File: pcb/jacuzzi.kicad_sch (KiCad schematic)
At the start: 56 parts, among them J1 Conn_01x02, J2 Conn_01x04, J3 Conn_01x03, J4 Conn_01x04, J5 Conn_01x03, J6 Conn_01x03, J7 Conn_01x02, J8 Conn_01x08, K1 G5LE-1, Q1 IRF4905, Q2 BC547, Q3 BC547, Q4 IRF4905, Q5 BC547, Q6 BC547

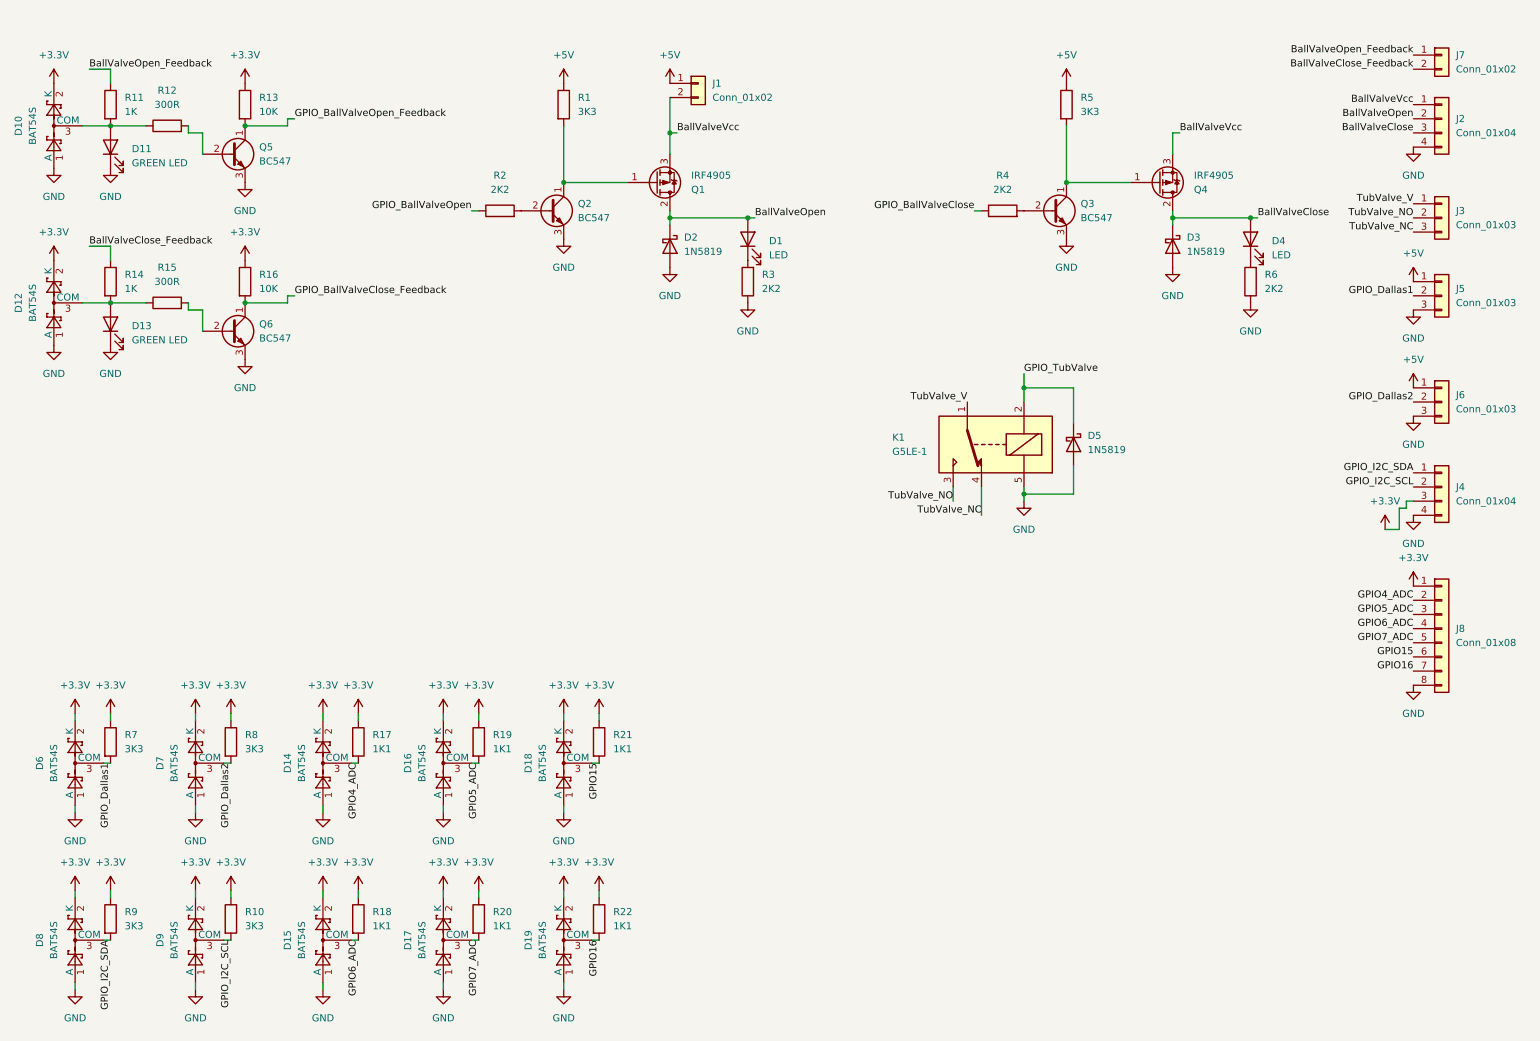
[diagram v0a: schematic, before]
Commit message: now using l293dd
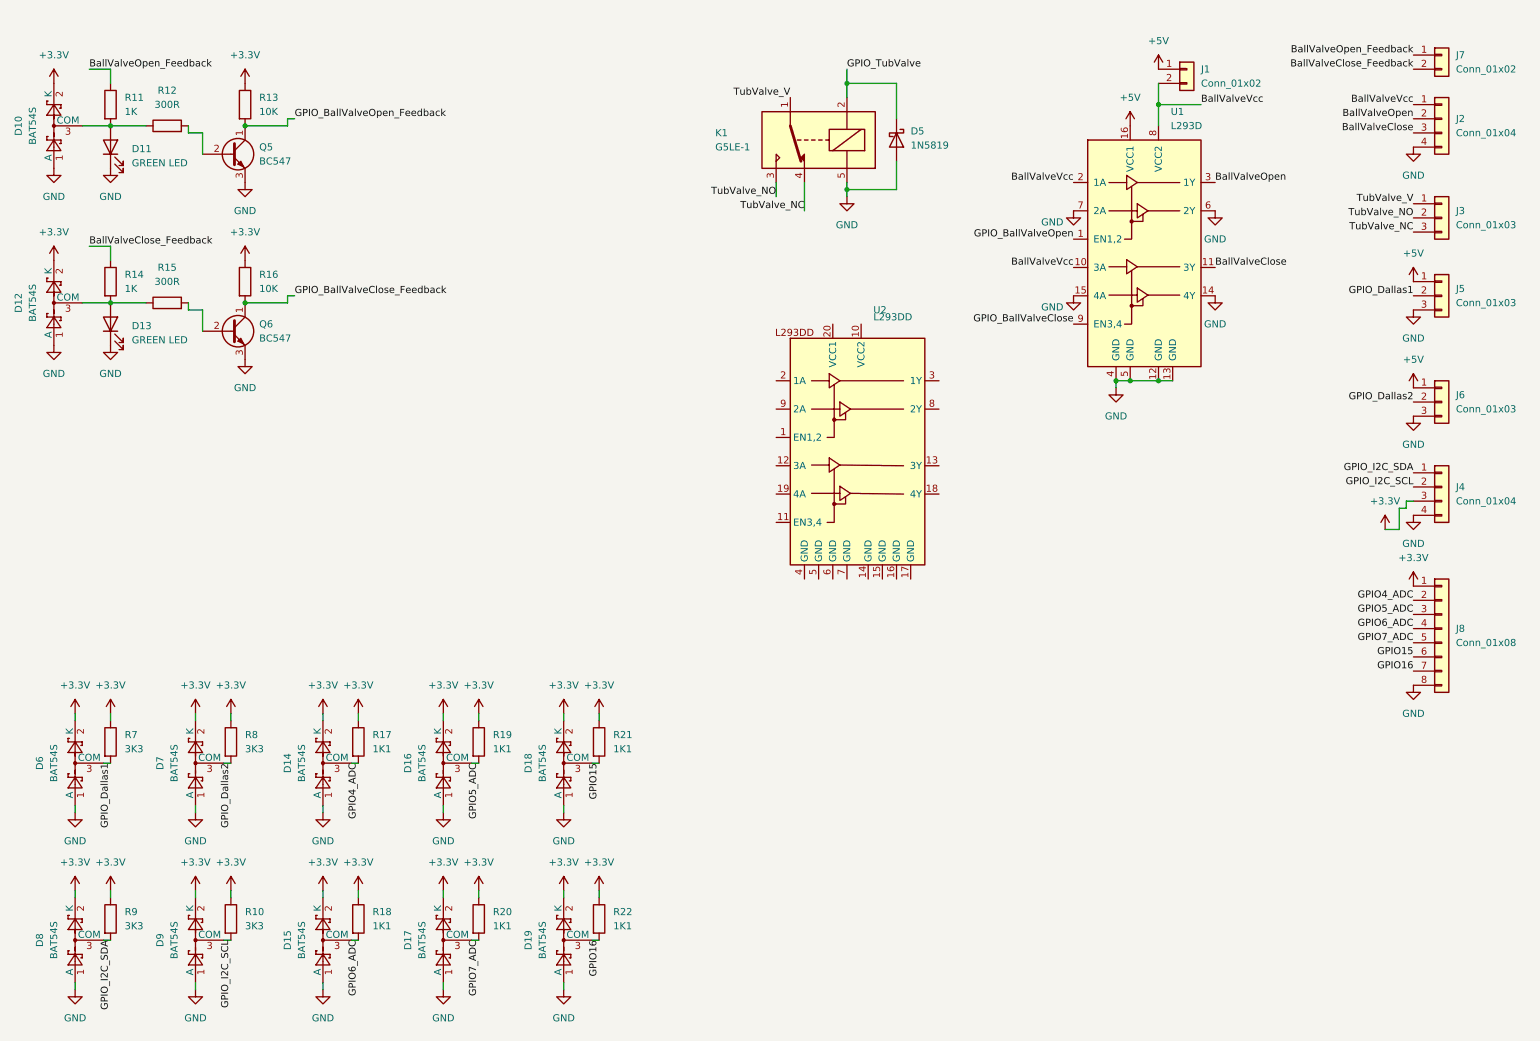
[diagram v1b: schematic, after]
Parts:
- removed D1, D4: LED, symbol Device:LED
- removed D2, D3: 1N5819, Diode_SMD:D_SOD-323, symbol Device:D_Schottky
- removed Q1, Q4: IRF4905, Package_TO_SOT_THT:TO-220-3_Vertical, symbol Transistor_FET:IRF4905
- removed Q2, Q3: BC547, Package_TO_SOT_THT:TO-92_Inline, symbol Transistor_BJT:BC547
- removed R1, R5: 3K3, Resistor_SMD:R_0805_2012Metric, symbol Device:R
- removed R2, R3, R4, R6: 2K2, Resistor_SMD:R_0805_2012Metric, symbol Device:R
- added U1: L293D, Package_SO:SOIC-20W_7.5x12.8mm_P1.27mm, symbol Driver_Motor:L293D
- added U2: L293DD, Package_SO:SOIC-20W_7.5x12.8mm_P1.27mm, symbol my_custom_library:L293DD
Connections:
- net +5V: now also U1.16 (VCC1)
- net BallValveClose: now also U1.11 (3Y)
- net BallValveOpen: now also U1.3 (1Y)
- net BallValveVcc: now also U1.10 (3A), U1.2 (1A), U1.8 (VCC2)
- net GND: now also U1.12 (GND), U1.13 (GND), U1.14 (4Y), U1.15 (4A), U1.4 (GND), U1.5 (GND), U1.6 (2Y), U1.7 (2A)
- net GPIO_BallValveClose: now also U1.9 (EN3,4)
- net GPIO_BallValveOpen: now also U1.1 (EN1,2)
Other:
- moved on the sheet: D5, K1

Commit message: testing if fymbols and foot print work when added to project
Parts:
- added U3: ESP32-DEVKITC-32U, ESP32-DEVKITC-32U:MODULE_ESP32-DEVKITC-32U, symbol ESP32-DEVKITC-32U:ESP32-DEVKITC-32U

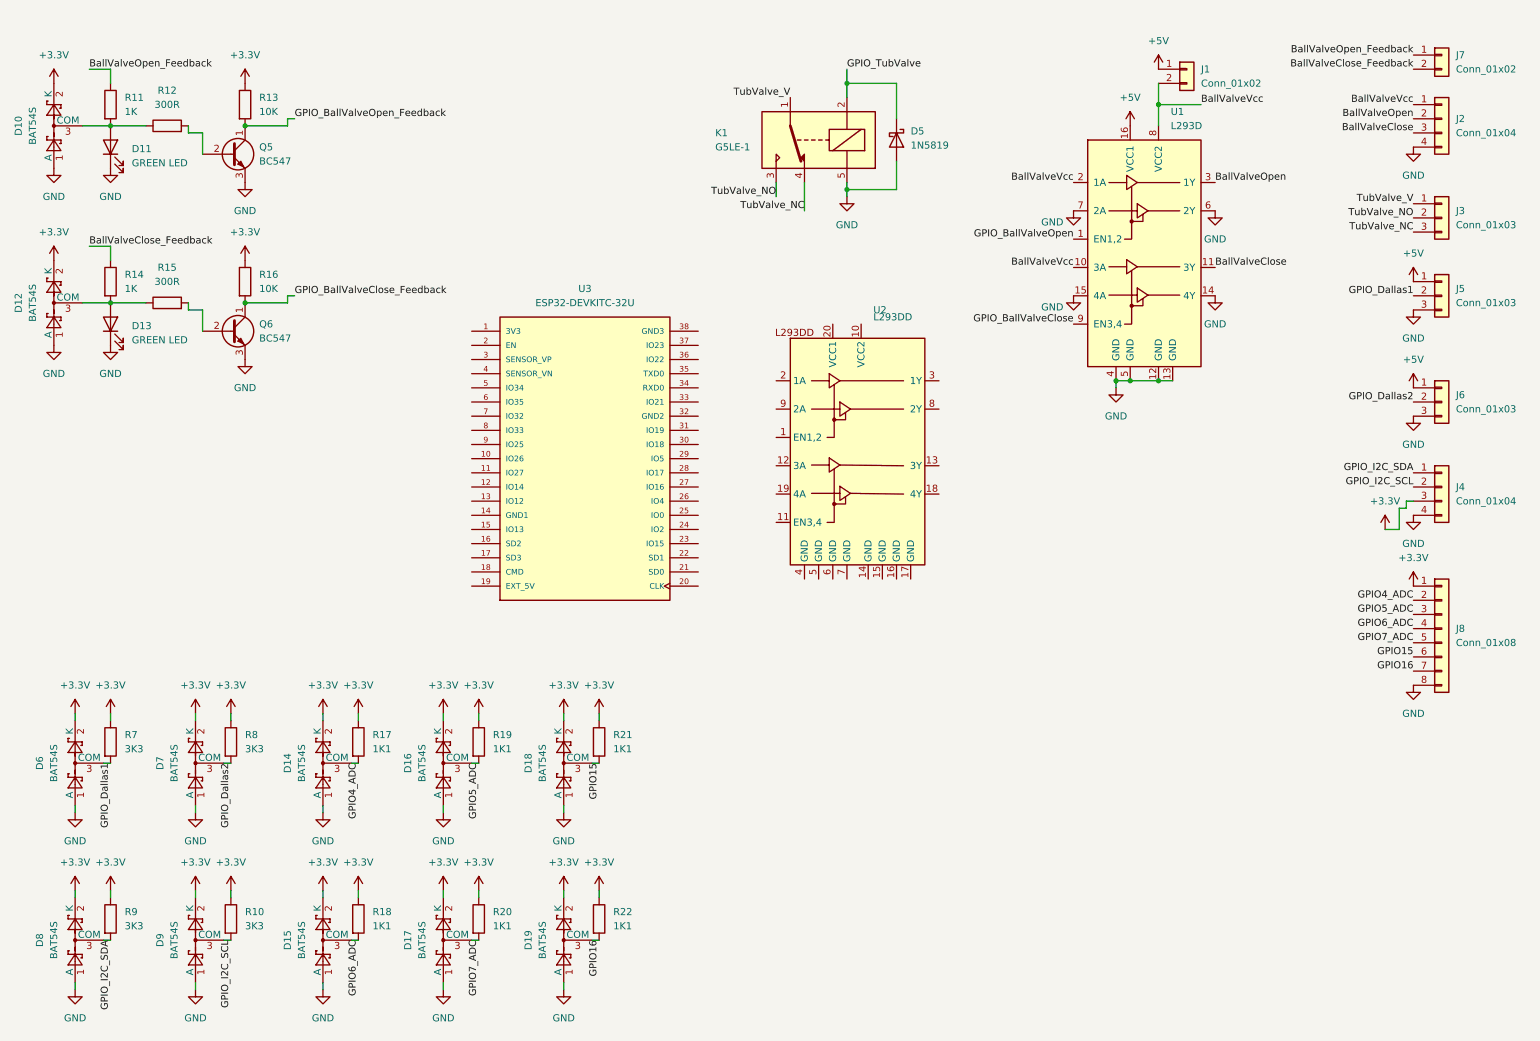
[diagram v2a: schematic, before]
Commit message: use cheap p channels instead of motor circuit, add usb c, add buck converter, switch to smd bjts
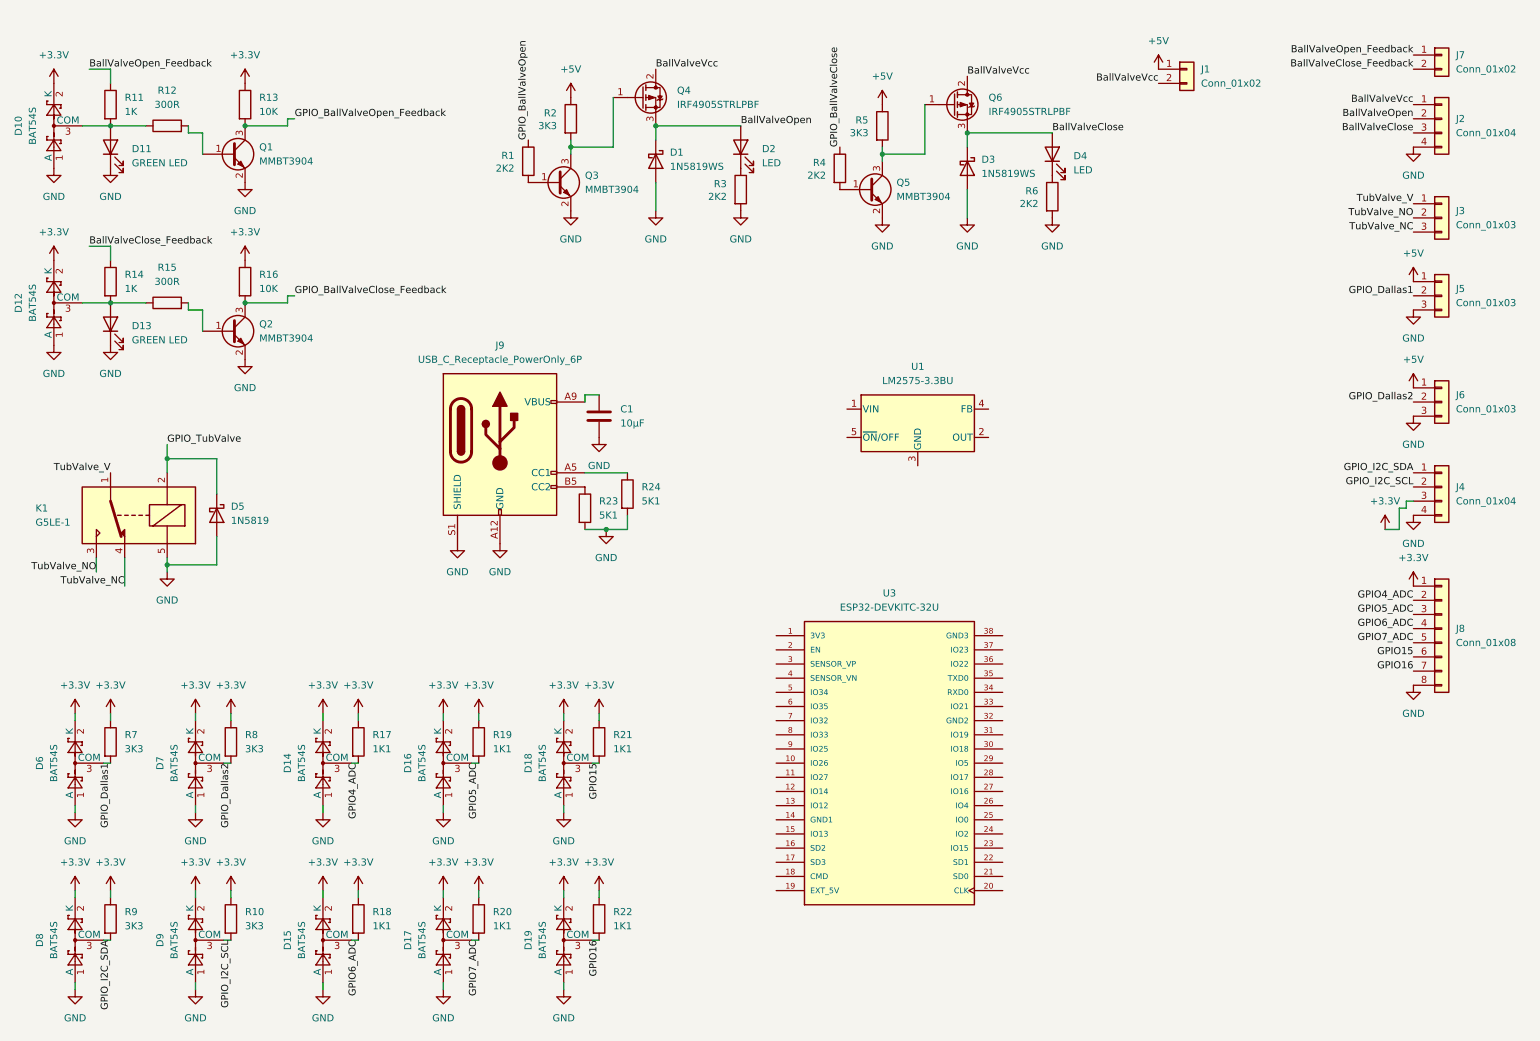
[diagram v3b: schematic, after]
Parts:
- removed Q5, Q6: BC547, Package_TO_SOT_THT:TO-92_Inline, symbol Transistor_BJT:BC547
- removed U1: L293D, Package_SO:SOIC-20W_7.5x12.8mm_P1.27mm, symbol Driver_Motor:L293D
- removed U2: L293DD, Package_SO:SOIC-20W_7.5x12.8mm_P1.27mm, symbol my_custom_library:L293DD
- added C1: 10µF, Capacitor_SMD:C_0805_2012Metric, symbol Device:C
- added D1, D3: 1N5819WS, Diode_SMD:D_SOD-323, symbol Diode:1N5819WS
- added D2, D4: LED, symbol Device:LED
- added J9: USB_C_Receptacle_PowerOnly_6P, Connector_USB:USB_C_Receptacle_GCT_USB4135-GF-A_6P_TopMnt_Horizontal, symbol Connector:USB_C_Receptacle_PowerOnly_6P
- added Q1, Q2, Q3, Q5: MMBT3904, Package_TO_SOT_SMD:SOT-23, symbol Transistor_BJT:MMBT3904
- added Q4, Q6: IRF4905STRLPBF, Package_TO_SOT_SMD:TO-263-2, symbol Transistor_FET:IRF4905
- added R1, R3, R4, R6: 2K2, Resistor_SMD:R_0805_2012Metric, symbol Device:R
- added R2, R5: 3K3, Resistor_SMD:R_0805_2012Metric, symbol Device:R
- added R23, R24: 5K1, Resistor_SMD:R_0805_2012Metric, symbol Device:R
- added U1: LM2575-3.3BU, Package_TO_SOT_SMD:TO-263-5_TabPin3, symbol Regulator_Switching:LM2575-3.3BU
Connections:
- net +5V: now also R2.1, R5.1
- net BallValveClose: now also D3.1 (K), D4.2 (A), Q6.3 (S)
- net BallValveOpen: now also D1.1 (K), D2.2 (A), Q4.3 (S)
- net BallValveVcc: now also Q4.2 (D), Q6.2 (D)
- net GND: now also C1.2, D1.2 (A), D3.2 (A), J9.A12 (GND), J9.B12 (GND), J9.S1 (SHIELD), Q1.2 (E), Q2.2 (E), Q3.2 (E), Q5.2 (E), R23.2, R24.2, R3.2, R6.2
- net GPIO_BallValveClose: now also R4.1
- net GPIO_BallValveClose_Feedback: now also Q2.3 (C)
- net GPIO_BallValveOpen: now also R1.1
- net GPIO_BallValveOpen_Feedback: now also Q1.3 (C)
- net at R15.2: now also Q2.1 (B)
- net at R12.2: now also Q1.1 (B)
- new net: C1.1, J9.A9 (VBUS), J9.B9 (VBUS)
- new net: D2.1 (K), R3.1
- new net: Q3.1 (B), R1.2
- new net: Q3.3 (C), Q4.1 (G), R2.2
- new net: Q5.1 (B), R4.2
- new net: J9.B5 (CC2), R23.1
- new net: Q5.3 (C), Q6.1 (G), R5.2
- new net: D4.1 (K), R6.1
- new net: J9.A5 (CC1), R24.1
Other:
- moved on the sheet: D5, K1, U3

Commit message: add around buck converter
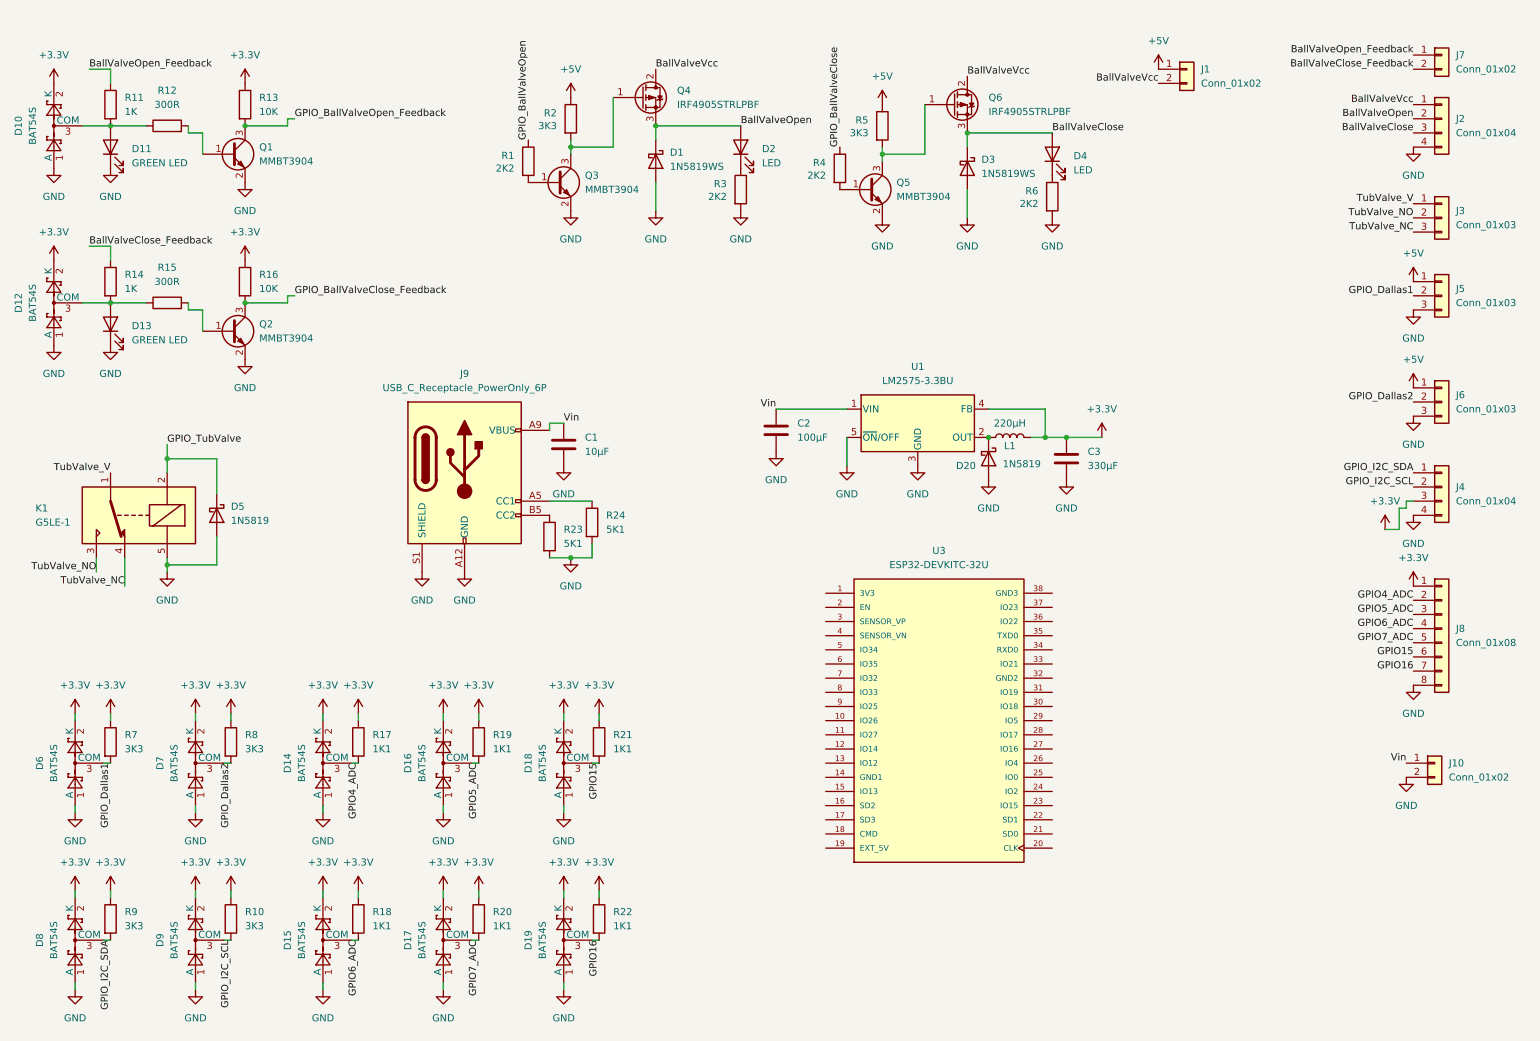
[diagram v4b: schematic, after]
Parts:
- added C2: 100µF, Capacitor_SMD:CP_Elec_8x10, symbol Device:C
- added C3: 330µF, Capacitor_SMD:CP_Elec_6.3x7.7, symbol Device:C
- added D20: 1N5819, Diode_SMD:D_SOD-323, symbol Device:D_Schottky
- added J10: Conn_01x02, symbol Connector_Generic:Conn_01x02
- added L1: 220µH, Inductor_SMD:L_Sunlord_SWRB1207S, symbol Device:L
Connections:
- net +3.3V: now also U1.4 (FB), C3.1, L1.2
- net GND: now also U1.3 (GND), U1.5 (~{ON}/OFF), C2.2, C3.2, D20.2 (A), J10.2 (Pin_2)
- net Vin: now reaches U1.1 (VIN)
- net Vin: now also C1.1, J9.A9 (VBUS), J9.B9 (VBUS), C2.1, J10.1 (Pin_1)
- net at U1.2 (OUT): now also D20.1 (K), L1.1
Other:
- moved on the sheet: C1, J9, R23, R24, U3

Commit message: wip
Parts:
- removed J1: Conn_01x02, Connector_PinHeader_2.54mm:PinHeader_1x02_P2.54mm_Vertical, symbol Connector_Generic:Conn_01x02
- removed J2: Conn_01x04, symbol Connector_Generic:Conn_01x04
- added C4: 100µF, Capacitor_SMD:CP_Elec_8x10, symbol Device:C
- added C5: 330µF, Capacitor_SMD:CP_Elec_6.3x7.7, symbol Device:C
- added D21: 1N5819, Diode_SMD:D_SOD-323, symbol Device:D_Schottky
- added D22, D23: 20V, Diode_SMD:D_SOD-323, symbol Device:D_Zener
- added D24: BAT54S, Package_TO_SOT_SMD:SOT-23, symbol Diode:BAT54S
- added J1, J2: Conn_01x03, Connector_Phoenix_MC:PhoenixContact_MCV_1,5_3-G-3.81_1x03_P3.81mm_Vertical, symbol Connector_Generic:Conn_01x03
- added L2: 330µH, Inductor_SMD:L_Sunlord_SWRB1207S, symbol Device:L
- added R25, R26: 330, Resistor_SMD:R_0805_2012Metric, symbol Device:R
- added R27: 1K1, Resistor_SMD:R_0805_2012Metric, symbol Device:R
- added U2: LM2575-5.0BU, Package_TO_SOT_SMD:TO-263-5_TabPin3, symbol Regulator_Switching:LM2575-5.0BU
- R1, R4: value 2K2 -> 1K
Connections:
- net +3.3V: now also D24.2 (K), R27.1
- net +5V: now also C1.1, J9.A9 (VBUS), J9.B9 (VBUS), C5.1, J2.1 (Pin_1), L2.2, U2.4 (FB); no longer R2.1, R5.1
- net BallValveClose: now also J1.2 (Pin_2)
- net BallValveOpen: now also J1.1 (Pin_1)
- net GND: now also C4.2, C5.2, D21.2 (A), D24.1 (A), J1.3 (Pin_3), J2.3 (Pin_3), R25.2, R26.2, U2.3 (GND), U2.5 (~{ON}/OFF); no longer Q3.2 (E), Q5.2 (E)
- net at Q3.3 (C), Q4.1 (G), R2.2: now also D22.2 (A)
- net at Q5.3 (C), Q6.1 (G), R5.2: now also D23.2 (A)
- net BallValveVcc renamed VS
- net VS: now also C2.1, J10.1 (Pin_1), R2.1, R5.1, U1.1 (VIN), C4.1, D22.1 (K), D23.1 (K), U2.1 (VIN)
- removed net Vin: C1.1, C2.1, J10.1 (Pin_1), J9.A9 (VBUS), J9.B9 (VBUS), U1.1 (VIN)
- new net: D21.1 (K), L2.1, U2.2 (OUT)
- new net: Q3.2 (E), R25.1
- new net: Q5.2 (E), R26.1
- new net GPIO_Servo: D24.3 (COM), J2.2 (Pin_2), R27.2
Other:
- moved on the sheet: C1, C2, C3, D1, D2, D20, D3, D4, J10, J4, J8, J9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
